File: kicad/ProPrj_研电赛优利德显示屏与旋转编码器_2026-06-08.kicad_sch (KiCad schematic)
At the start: 17 parts, among them Q1 S8050, SW1 EC11N1525405

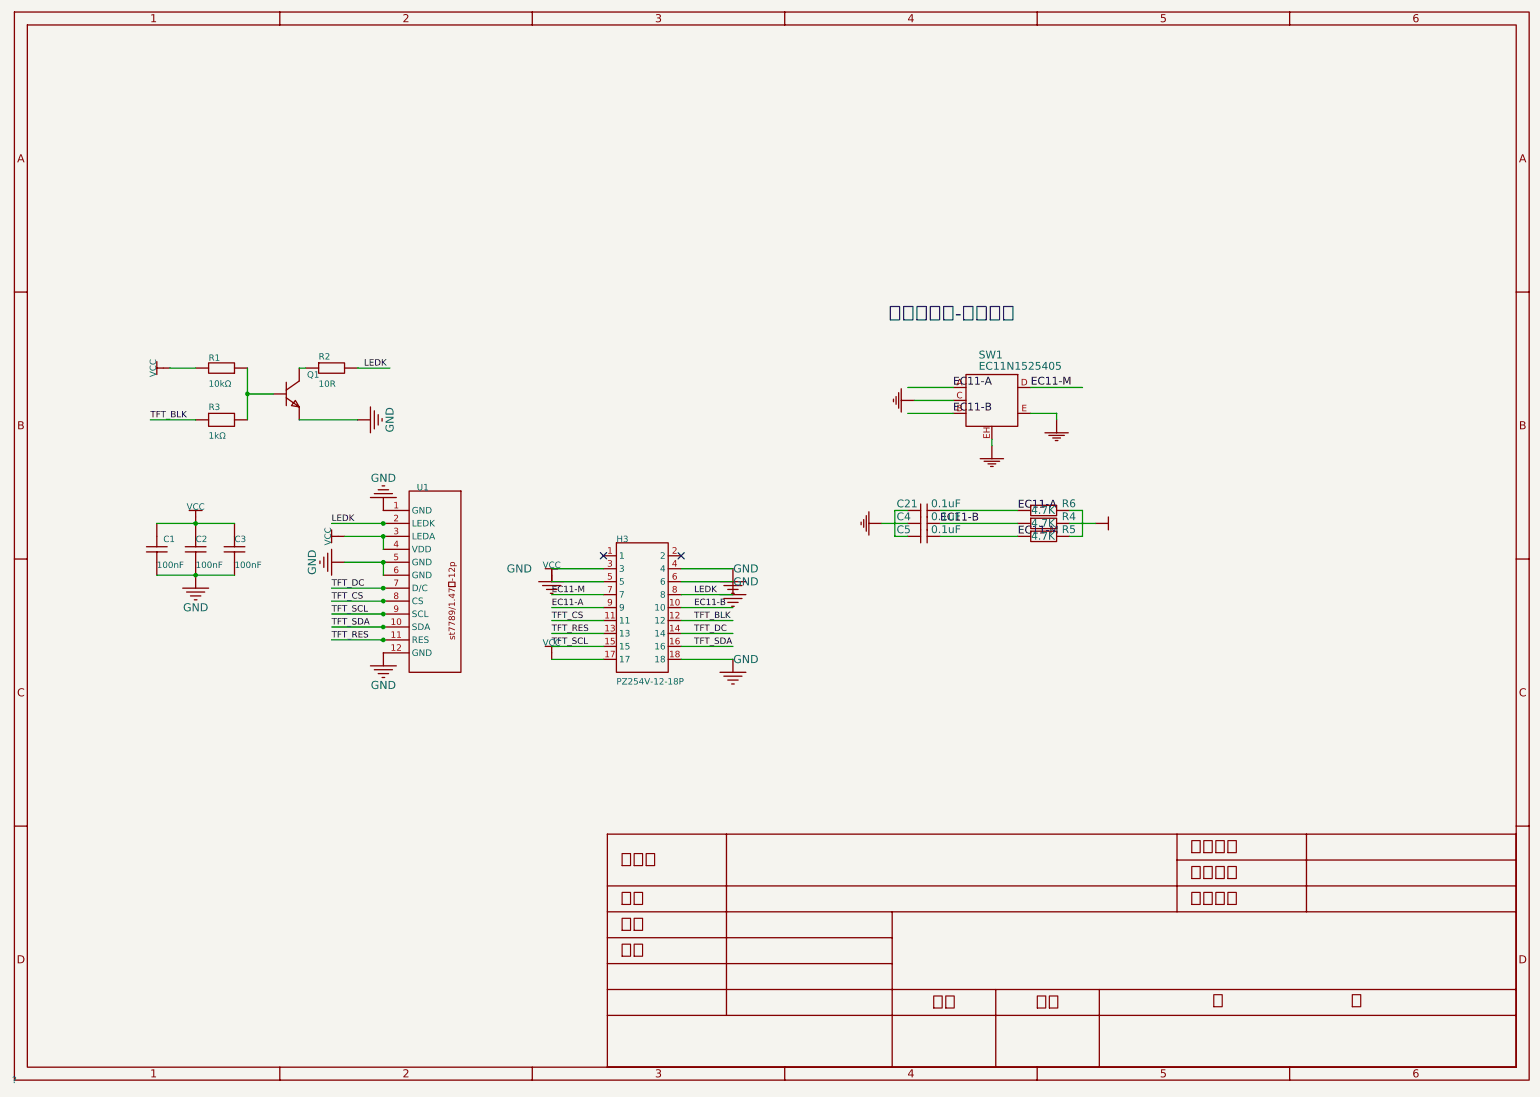
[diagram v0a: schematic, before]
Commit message: docs: comprehensive FMC signal mapping and cleanup
1. FMC signal documentation:
   - Create docs/fmc_adda_signal_map.md - complete daughter card to
     baseboard signal mapping table (verified from both PDF manuals)
   - Update README.md to reflect current project state

2. Fix LMK04828 pin assignments (was using wrong I2C pins):
   - lmk04828_spi_sclk: AD29 -> E16 (LA29_N, ADK_SCLK)
   - lmk04828_spi_sdio: AE29 -> J12 (LA28_N, ADK_SDIO)
   - lmk04828_cs_n:     (new) -> J11 (LA28_P, ADK_CSB)
   - lmk04828_reset:    (new) -> F15 (LA29_P, ADK_RST)
   Verified from baseboard schematic K7_BASE_1V3_2025_0111_USER.pdf

3. Remove DRC override (UCIO-1/NSTD-1) - all pins now assigned

4. Clean up redundant docs:
   - Remove docs/superpowers/plans/ (8 outdated planning docs)
   - Remove docs/agents/development_log.md (redundant with git log)
   - Remove root-level AGENTS.md, K325T_AWG_*.md (outdated architecture)

Co-Authored-By: Claude Opus 4.8 <noreply@anthropic.com>
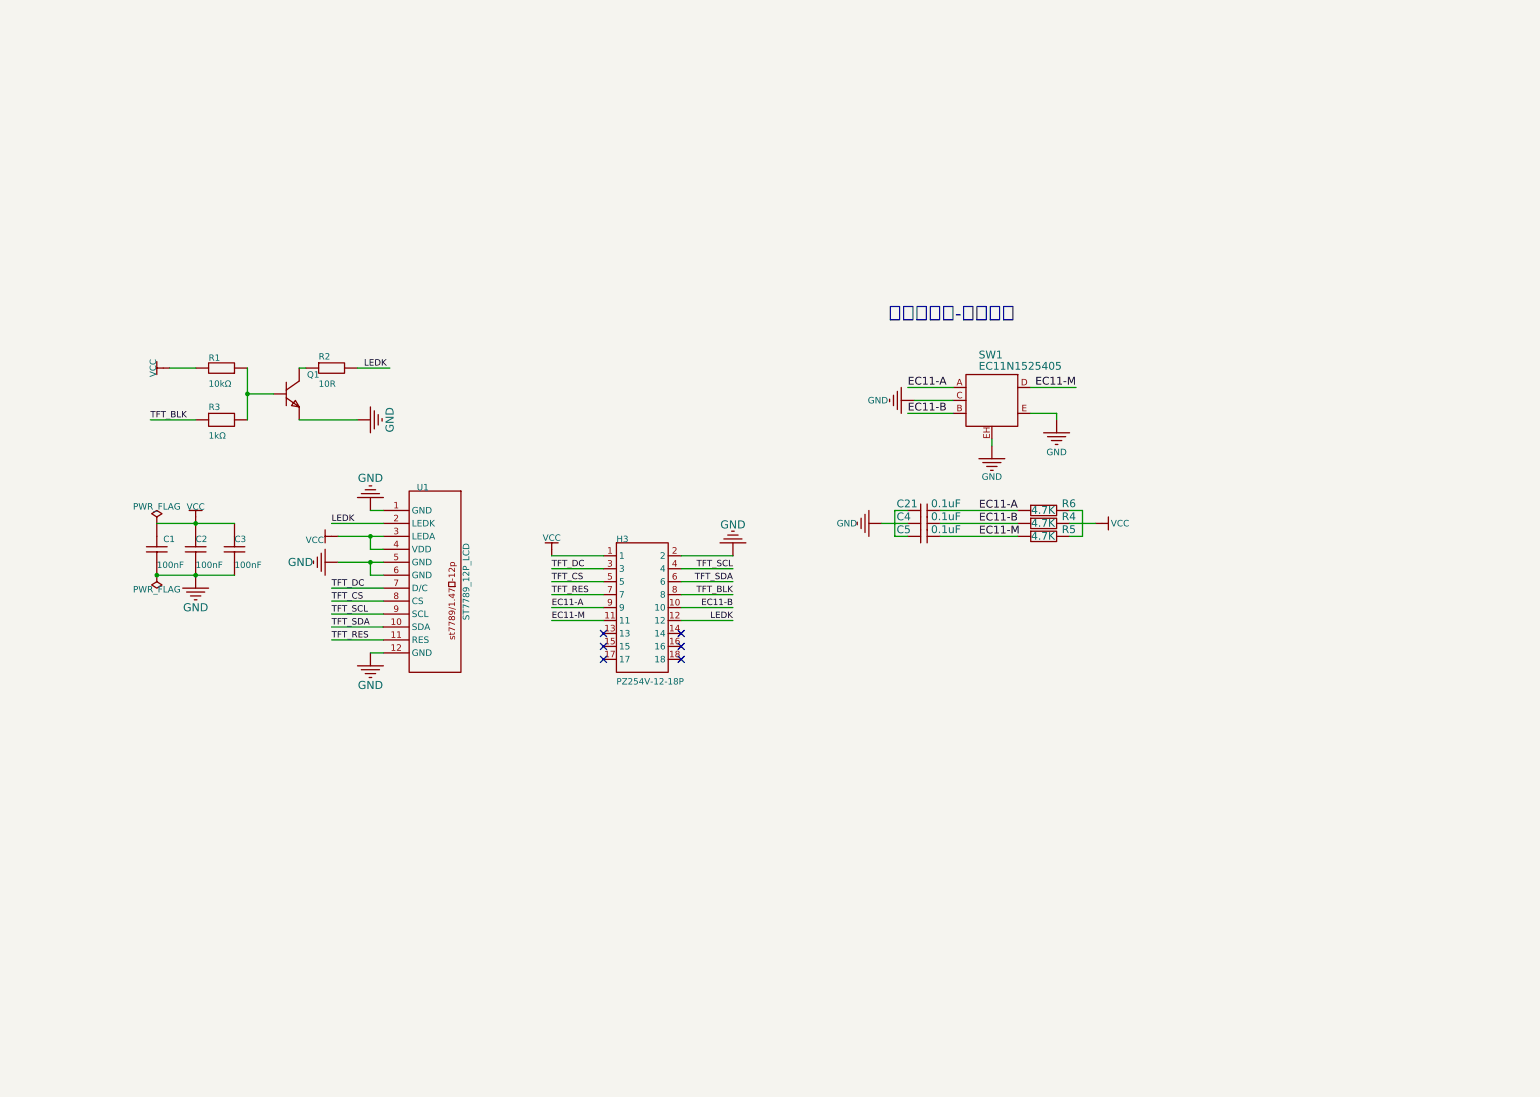
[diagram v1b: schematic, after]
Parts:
- removed ?: (no value), ProPrj_研电赛-easyedapro:, symbol ProPrj_研电赛-easyedapro:Sheet-Symbol_A4
- C21, C4, C5: footprint ProPrj_研电赛-easyedapro: -> ProPrj_研电赛-easyedapro:C0603
- R2, R4, R5, R6: footprint ProPrj_研电赛-easyedapro: -> ProPrj_研电赛-easyedapro:R0603
- SW1: footprint ProPrj_研电赛-easyedapro: -> ProPrj_研电赛-easyedapro:EC11_ROTARY_ENCODER
- U1: value (none) -> ST7789_12P_LCD; footprint ProPrj_研电赛-easyedapro:st7789/1.69寸-12p -> ProPrj_研电赛-easyedapro:ST7789_12P_1x12_1.00mm
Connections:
- net EC11-M: now also H3.11; no longer H3.7
- net GND: now also C4.1, H3.2, SW1.C, SW1.E, SW1.EH, U1.1 (GND), U1.12 (GND), U1.6 (GND); no longer H3.18, H3.3, H3.4, H3.6
- net LEDK: now also H3.12; no longer H3.8
- net TFT_BLK: now also H3.8; no longer H3.12
- net TFT_CS: now also H3.5; no longer H3.11
- net TFT_DC: now also H3.3; no longer H3.14
- net TFT_RES: now also H3.7; no longer H3.13
- net TFT_SCL: now also H3.4; no longer H3.15
- net TFT_SDA: now also H3.6; no longer H3.16
- net VCC: now also H3.1, R4.2, U1.4 (VDD); no longer H3.17, H3.5
- no-connect marks 2 -> 6
